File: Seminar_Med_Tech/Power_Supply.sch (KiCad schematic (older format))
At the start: 35 parts, among them U2 LM317T, U3 LM317T, U4 LM317T, U5 LM317T, U6 LM337K

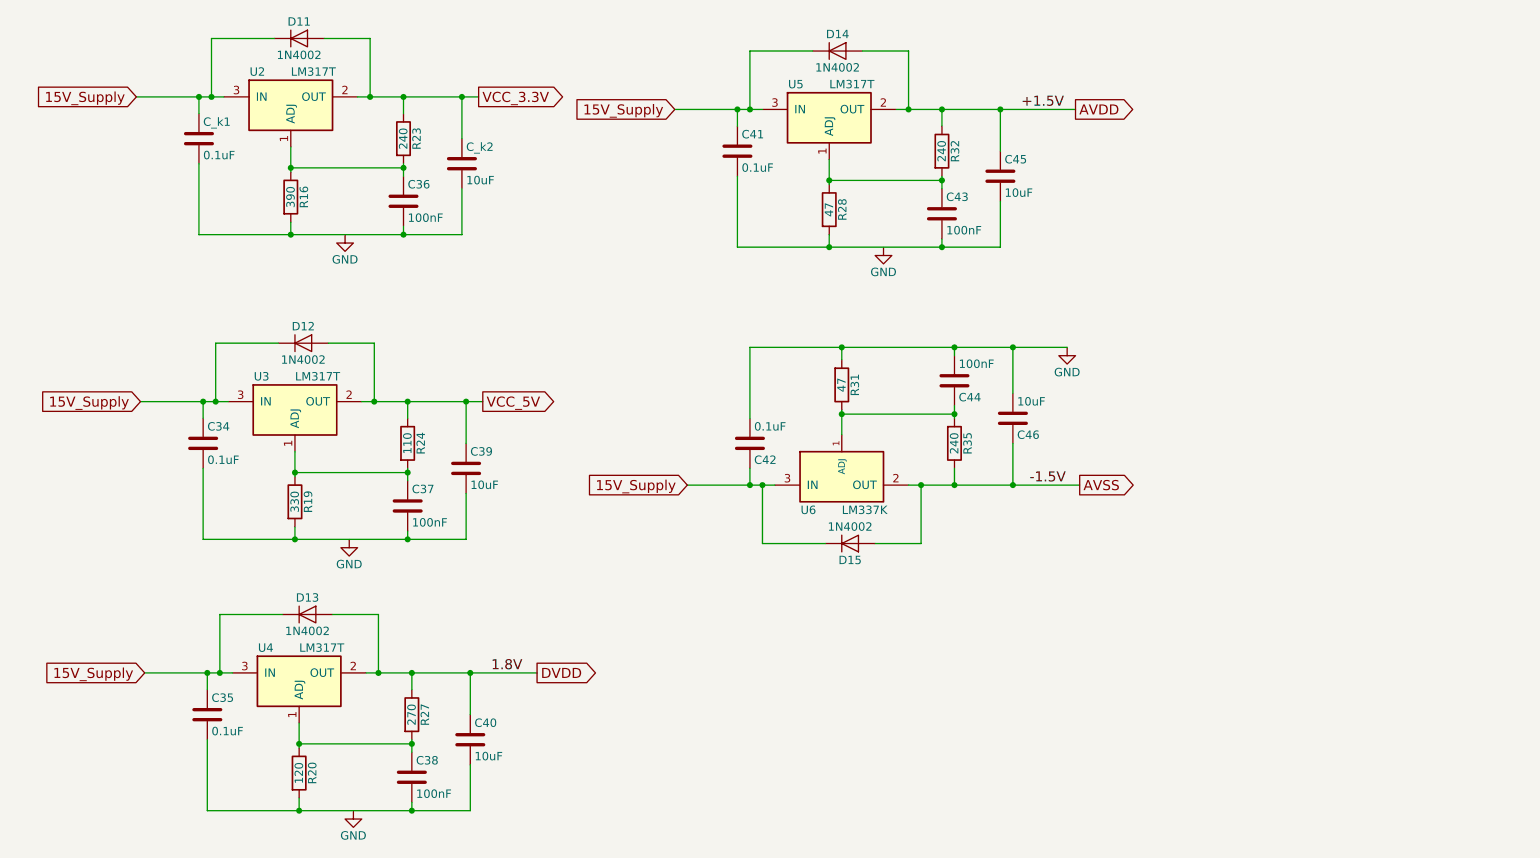
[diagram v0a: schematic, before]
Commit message: Updated Schaltbild and changed BOM
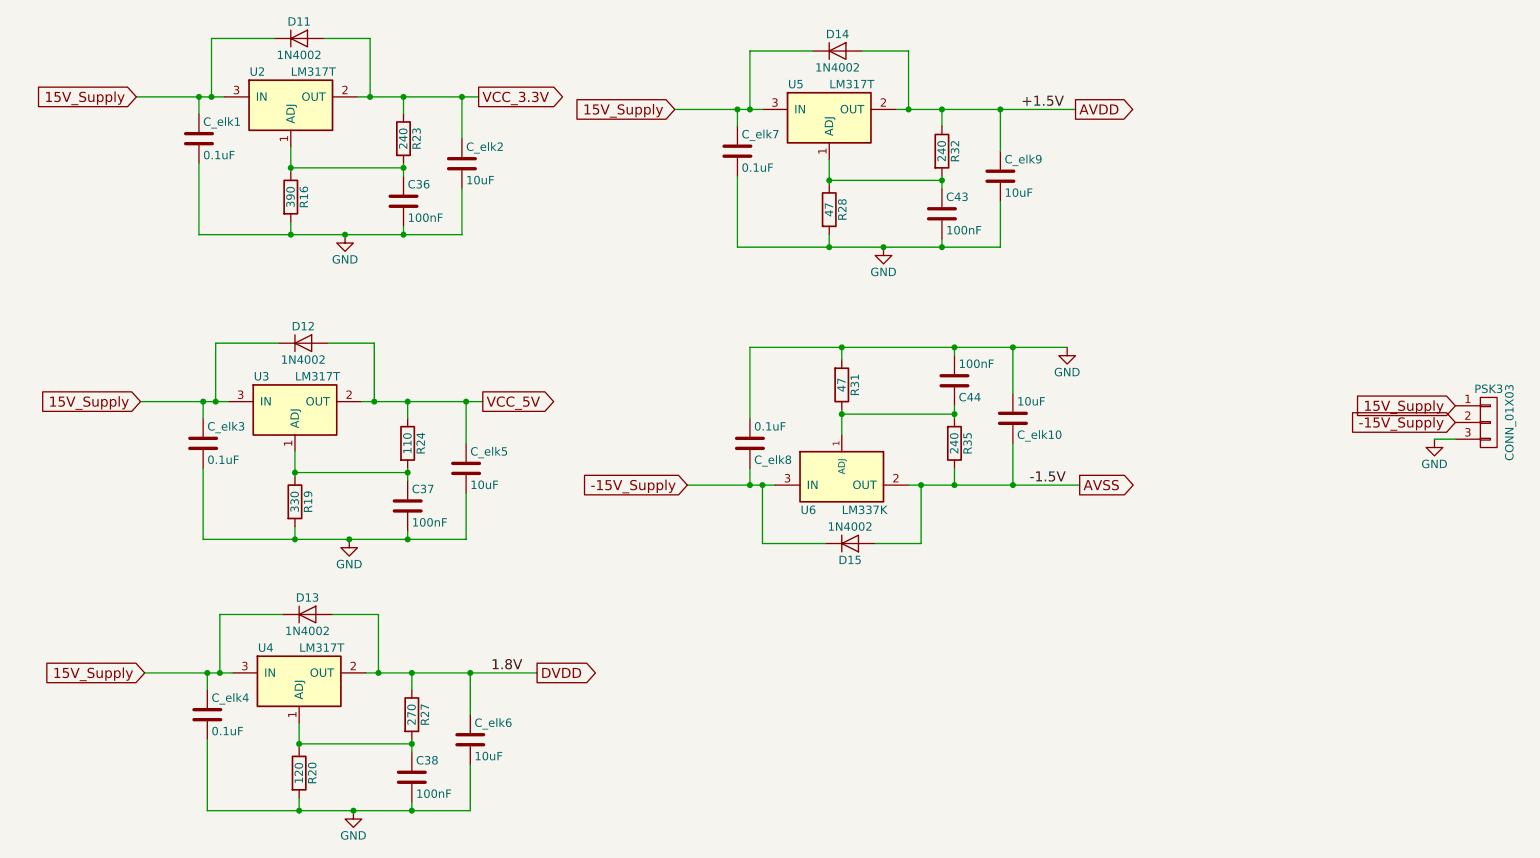
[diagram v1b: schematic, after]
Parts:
- added PSK3: CONN_01X03, symbol CONN_01X03
- renumbered C_k1 to C_elk1, C46 to C_elk10, C_k2 to C_elk2, C34 to C_elk3, C35 to C_elk4, C39 to C_elk5, C40 to C_elk6, C41 to C_elk7, C42 to C_elk8, C45 to C_elk9
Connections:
- net 15V_Supply: now also PSK3.1 (P1); no longer C_elk8.1, D15.1 (K), U6.3 (IN)
- net GND: now also C36.2, C37.2, C38.2, C43.2, C_elk1.2, C_elk2.2, C_elk3.2, C_elk4.2, C_elk5.2, C_elk6.2, C_elk7.2, C_elk9.2, R16.2, R19.2, R20.2, R28.2, PSK3.3 (P3)
- new net -15V_Supply: C_elk8.1, D15.1 (K), PSK3.2 (P2), U6.3 (IN)

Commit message: Updated Schaltbild and added LM317 footprint
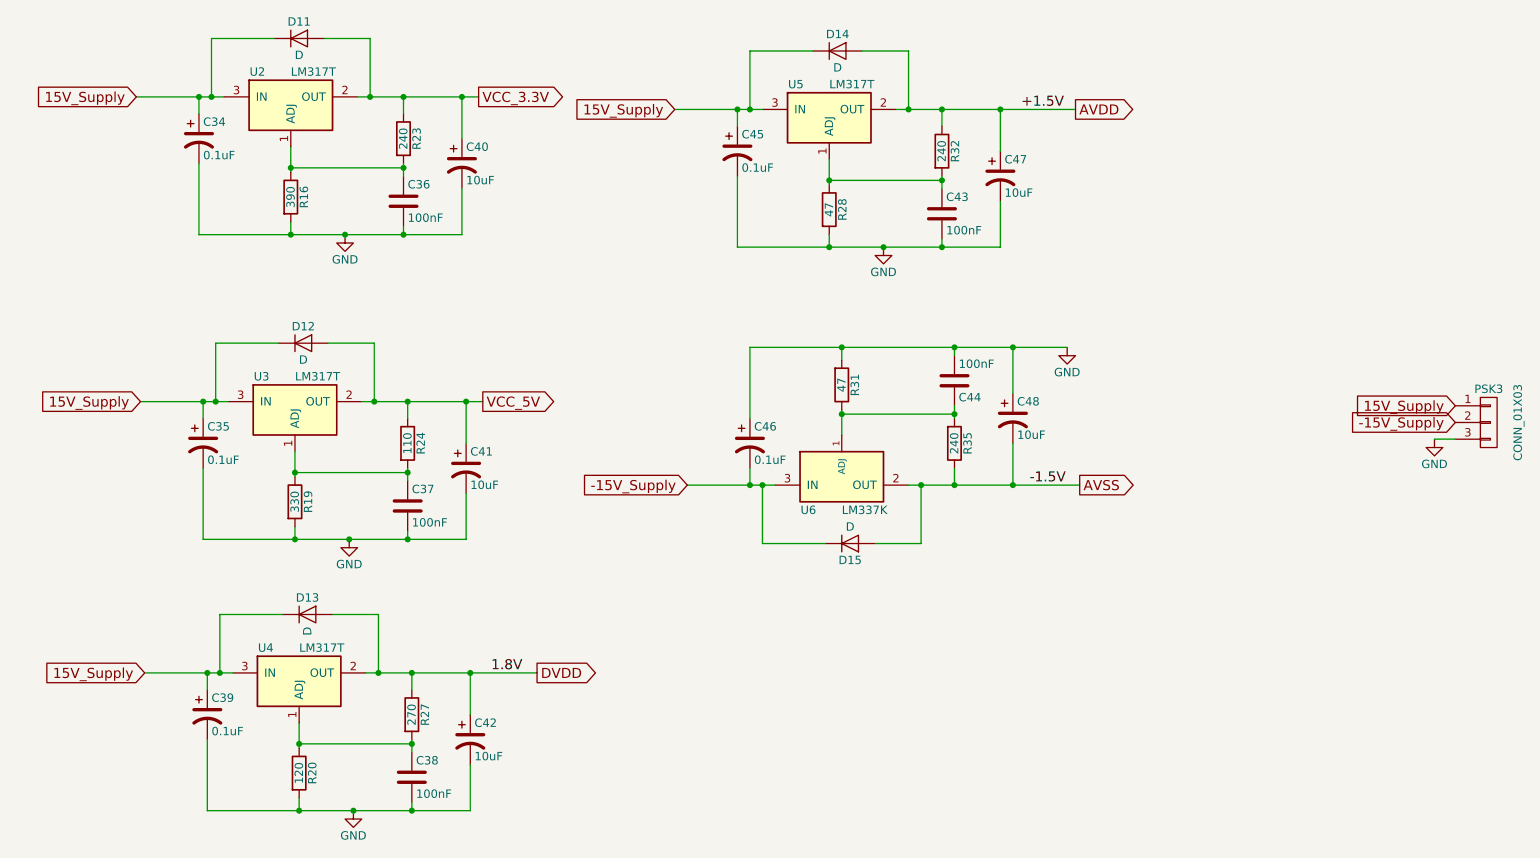
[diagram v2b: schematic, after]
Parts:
- removed C_elk1, C_elk3, C_elk4, C_elk7, C_elk8: 0.1uF, Capacitors_SMD:C_1206_HandSoldering, symbol C
- removed C_elk10, C_elk2, C_elk5, C_elk6, C_elk9: 10uF, Capacitors_SMD:C_1206_HandSoldering, symbol C
- added C34, C35, C39, C45, C46: 0.1uF, Capacitors_SMD:CP_Elec_4x5.8, symbol CP1
- added C40, C41, C42, C47, C48: 10uF, Capacitors_SMD:CP_Elec_4x5.8, symbol CP1
- D11, D12, D13, D14, D15: value 1N4002 -> D
- PSK3: footprint (none) -> Pin_Headers:Pin_Header_Straight_1x03_Pitch2.54mm
- U2, U3, U4, U5: footprint TO_SOT_Packages_THT:TO-220_Vertical -> Linear_Regulator:LM317
- U6: footprint TO_SOT_Packages_THT:TO-3 -> Linear_Regulator:LM317
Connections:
- net -15V_Supply: now also C46.2
- net 15V_Supply: now also C34.1, C35.1, C39.1, C45.1
- net AVDD: now also C47.1
- net AVSS: now also C48.2
- net DVDD: now also C42.1
- net GND: now also C34.2, C35.2, C39.2, C40.2, C41.2, C42.2, C45.2, C46.1, C47.2, C48.1
- net VCC_3.3V: now also C40.1
- net VCC_5V: now also C41.1
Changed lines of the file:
@@
 F 0 "U2" H 2600 1700 50  0000 C CNN
 F 1 "LM317T" H 2800 1700 50  0000 L CNN
-F 2 "TO_SOT_Packages_THT:TO-220_Vertical" H 2800 1600 50  0001 C CIN
+F 2 "Linear_Regulator:LM317" H 2800 1600 50  0001 C CIN
 F 3 "" H 2800 1500 50  0001 C CNN
 	1    2800 1500
-	1    0    0    -1
-$EndComp
-$Comp
-L C C_elk1
-U 1 1 5947F15B
-P 2250 1700
-F 0 "C_elk1" H 2275 1800 50  0000 L CNN
-F 1 "0.1uF" H 2275 1600 50  0000 L CNN
-F 2 "Capacitors_SMD:C_1206_HandSoldering" H 2288 1550 50  0001 C CNN
-F 3 "" H 2250 1700 50  0001 C CNN
-	1    2250 1700
 	1    0    0    -1
 $EndComp
@@
 $EndComp
 $Comp
-L C C_elk2
-U 1 1 5947F1C2
-P 3825 1850
-F 0 "C_elk2" H 3850 1950 50  0000 L CNN
-F 1 "10uF" H 3850 1750 50  0000 L CNN
-F 2 "Capacitors_SMD:C_1206_HandSoldering" H 3863 1700 50  0001 C CNN
-F 3 "" H 3825 1850 50  0001 C CNN
-	1    3825 1850
-	1    0    0    -1
-$EndComp
-$Comp
 L D D11
 U 1 1 5947F210
 P 2850 1100
 F 0 "D11" H 2850 1200 50  0000 C CNN
-F 1 "1N4002" H 2850 1000 50  0000 C CNN
+F 1 "D" H 2850 1000 50  0000 C CNN
 F 2 "Diodes_SMD:D_SC-80_HandSoldering" H 2850 1100 50  0001 C CNN
 F 3 "" H 2850 1100 50  0001 C CNN
@@
 F 0 "U3" H 2625 3525 50  0000 C CNN
 F 1 "LM317T" H 2825 3525 50  0000 L CNN
-F 2 "TO_SOT_Packages_THT:TO-220_Vertical" H 2825 3425 50  0001 C CIN
+F 2 "Linear_Regulator:LM317" H 2825 3425 50  0001 C CIN
 F 3 "" H 2825 3325 50  0001 C CNN
 	1    2825 3325
-	1    0    0    -1
-$EndComp
-$Comp
-L C C_elk3
-U 1 1 59480213
-P 2275 3525
-F 0 "C_elk3" H 2300 3625 50  0000 L CNN
-F 1 "0.1uF" H 2300 3425 50  0000 L CNN
-F 2 "Capacitors_SMD:C_1206_HandSoldering" H 2313 3375 50  0001 C CNN
-F 3 "" H 2275 3525 50  0001 C CNN
-	1    2275 3525
 	1    0    0    -1
 $EndComp
@@
 $EndComp
 $Comp
-L C C_elk5
-U 1 1 5948021F
-P 3850 3675
-F 0 "C_elk5" H 3875 3775 50  0000 L CNN
-F 1 "10uF" H 3875 3575 50  0000 L CNN
-F 2 "Capacitors_SMD:C_1206_HandSoldering" H 3888 3525 50  0001 C CNN
-F 3 "" H 3850 3675 50  0001 C CNN
-	1    3850 3675
-	1    0    0    -1
-$EndComp
-$Comp
 L D D12
 U 1 1 59480225
 P 2875 2925
 F 0 "D12" H 2875 3025 50  0000 C CNN
-F 1 "1N4002" H 2875 2825 50  0000 C CNN
+F 1 "D" H 2875 2825 50  0000 C CNN
 F 2 "Diodes_SMD:D_SC-80_HandSoldering" H 2875 2925 50  0001 C CNN
 F 3 "" H 2875 2925 50  0001 C CNN
@@
 F 0 "U5" H 5825 1775 50  0000 C CNN
 F 1 "LM317T" H 6025 1775 50  0000 L CNN
-F 2 "TO_SOT_Packages_THT:TO-220_Vertical" H 6025 1675 50  0001 C CIN
+F 2 "Linear_Regulator:LM317" H 6025 1675 50  0001 C CIN
 F 3 "" H 6025 1575 50  0001 C CNN
 	1    6025 1575
-	1    0    0    -1
-$EndComp
-$Comp
-L C C_elk7
-U 1 1 59480A0E
-P 5475 1775
-F 0 "C_elk7" H 5500 1875 50  0000 L CNN
-F 1 "0.1uF" H 5500 1675 50  0000 L CNN
-F 2 "Capacitors_SMD:C_1206_HandSoldering" H 5513 1625 50  0001 C CNN
-F 3 "" H 5475 1775 50  0001 C CNN
-	1    5475 1775
 	1    0    0    -1
 $EndComp
@@
 $EndComp
 $Comp
-L C C_elk9
-U 1 1 59480A1A
-P 7050 1925
-F 0 "C_elk9" H 7075 2025 50  0000 L CNN
-F 1 "10uF" H 7075 1825 50  0000 L CNN
-F 2 "Capacitors_SMD:C_1206_HandSoldering" H 7088 1775 50  0001 C CNN
-F 3 "" H 7050 1925 50  0001 C CNN
-	1    7050 1925
-	1    0    0    -1
-$EndComp
-$Comp
 L D D14
 U 1 1 59480A20
 P 6075 1175
 F 0 "D14" H 6075 1275 50  0000 C CNN
-F 1 "1N4002" H 6075 1075 50  0000 C CNN
+F 1 "D" H 6075 1075 50  0000 C CNN
 F 2 "Diodes_SMD:D_SC-80_HandSoldering" H 6075 1175 50  0001 C CNN
 F 3 "" H 6075 1175 50  0001 C CNN
@@
 F 0 "U4" H 2650 5150 50  0000 C CNN
 F 1 "LM317T" H 2850 5150 50  0000 L CNN
-F 2 "TO_SOT_Packages_THT:TO-220_Vertical" H 2850 5050 50  0001 C CIN
+F 2 "Linear_Regulator:LM317" H 2850 5050 50  0001 C CIN
 F 3 "" H 2850 4950 50  0001 C CNN
 	1    2850 4950
-	1    0    0    -1
-$EndComp
-$Comp
-L C C_elk4
-U 1 1 59480B41
-P 2300 5150
-F 0 "C_elk4" H 2325 5250 50  0000 L CNN
-F 1 "0.1uF" H 2325 5050 50  0000 L CNN
-F 2 "Capacitors_SMD:C_1206_HandSoldering" H 2338 5000 50  0001 C CNN
-F 3 "" H 2300 5150 50  0001 C CNN
-	1    2300 5150
 	1    0    0    -1
 $EndComp
@@
 $EndComp
 $Comp
-L C C_elk6
-U 1 1 59480B4D
-P 3875 5300
-F 0 "C_elk6" H 3900 5400 50  0000 L CNN
-F 1 "10uF" H 3900 5200 50  0000 L CNN
-F 2 "Capacitors_SMD:C_1206_HandSoldering" H 3913 5150 50  0001 C CNN
-F 3 "" H 3875 5300 50  0001 C CNN
-	1    3875 5300
-	1    0    0    -1
-$EndComp
-$Comp
 L D D13
 U 1 1 59480B53
 P 2900 4550
 F 0 "D13" H 2900 4650 50  0000 C CNN
-F 1 "1N4002" H 2900 4450 50  0000 C CNN
+F 1 "D" V 2900 4450 50  0000 C CNN
 F 2 "Diodes_SMD:D_SC-80_HandSoldering" H 2900 4550 50  0001 C CNN
 F 3 "" H 2900 4550 50  0001 C CNN
@@
 F 0 "U6" H 5900 3525 50  0000 C CNN
 F 1 "LM337K" H 6100 3525 50  0000 L CNN
-F 2 "TO_SOT_Packages_THT:TO-3" H 6100 3625 50  0001 C CIN
+F 2 "Linear_Regulator:LM317" H 6100 3625 50  0001 C CIN
 F 3 "" H 6100 3725 50  0001 C CNN
 	1    6100 3725
@@
 Text GLabel 5175 3775 0    60   Input ~ 0
 -15V_Supply
-$Comp
-L C C_elk8
-U 1 1 5948C0A3
-P 5550 3525
-F 0 "C_elk8" H 5575 3625 50  0000 L CNN
-F 1 "0.1uF" H 5575 3425 50  0000 L CNN
-F 2 "Capacitors_SMD:C_1206_HandSoldering" H 5588 3375 50  0001 C CNN
-F 3 "" H 5550 3525 50  0001 C CNN
-	1    5550 3525
-	1    0    0    1
-$EndComp
 $Comp
 L C C44
@@
 $EndComp
 $Comp
-L C C_elk10
-U 1 1 5948C0AF
-P 7125 3375
-F 0 "C_elk10" H 7150 3475 50  0000 L CNN
-F 1 "10uF" H 7150 3275 50  0000 L CNN
-F 2 "Capacitors_SMD:C_1206_HandSoldering" H 7163 3225 50  0001 C CNN
-F 3 "" H 7125 3375 50  0001 C CNN
-	1    7125 3375
-	1    0    0    1
-$EndComp
-$Comp
 L D D15
 U 1 1 5948C0B5
 P 6150 4125
 F 0 "D15" H 6150 4225 50  0000 C CNN
-F 1 "1N4002" H 6150 4025 50  0000 C CNN
+F 1 "D" H 6150 4025 50  0000 C CNN
 F 2 "Diodes_SMD:D_SC-80_HandSoldering" H 6150 4125 50  0001 C CNN
 F 3 "" H 6150 4125 50  0001 C CNN
@@
 P 9975 3400
 F 0 "PSK3" H 9975 3600 50  0000 C CNN
-F 1 "CONN_01X03" V 10100 3400 50  0000 C CNN
-F 2 "" H 9975 3400 50  0001 C CNN
+F 1 "CONN_01X03" V 10150 3400 50  0000 C CNN
+F 2 "Pin_Headers:Pin_Header_Straight_1x03_Pitch2.54mm" H 9975 3400 50  0001 C CNN
 F 3 "" H 9975 3400 50  0001 C CNN
 	1    9975 3400
@@
 Wire Wire Line
 	9775 3500 9650 3500
+$Comp
+L CP1 C34
+U 1 1 594A8579
+P 2250 1700
+F 0 "C34" H 2275 1800 50  0000 L CNN
+F 1 "0.1uF" H 2275 1600 50  0000 L CNN
+F 2 "Capacitors_SMD:CP_Elec_4x5.8" H 2250 1700 50  0001 C CNN
+F 3 "" H 2250 1700 50  0001 C CNN
+	1    2250 1700
+	1    0    0    -1
+$EndComp
+$Comp
+L CP1 C40
+U 1 1 594A8C56
+P 3825 1850
+F 0 "C40" H 3850 1950 50  0000 L CNN
+F 1 "10uF" H 3850 1750 50  0000 L CNN
+F 2 "Capacitors_SMD:CP_Elec_4x5.8" H 3825 1850 50  0001 C CNN
+F 3 "" H 3825 1850 50  0001 C CNN
+	1    3825 1850
+	1    0    0    -1
+$EndComp
+$Comp
+L CP1 C35
+U 1 1 594AC0E4
+P 2275 3525
+F 0 "C35" H 2300 3625 50  0000 L CNN
+F 1 "0.1uF" H 2300 3425 50  0000 L CNN
+F 2 "Capacitors_SMD:CP_Elec_4x5.8" H 2275 3525 50  0001 C CNN
+F 3 "" H 2275 3525 50  0001 C CNN
+	1    2275 3525
+	1    0    0    -1
+$EndComp
+$Comp
+L CP1 C39
+U 1 1 594AC187
+P 2300 5150
+F 0 "C39" H 2325 5250 50  0000 L CNN
+F 1 "0.1uF" H 2325 5050 50  0000 L CNN
+F 2 "Capacitors_SMD:CP_Elec_4x5.8" H 2300 5150 50  0001 C CNN
+F 3 "" H 2300 5150 50  0001 C CNN
+	1    2300 5150
+	1    0    0    -1
+$EndComp
+$Comp
+L CP1 C45
+U 1 1 594AC237
+P 5475 1775
+F 0 "C45" H 5500 1875 50  0000 L CNN
+F 1 "0.1uF" H 5500 1675 50  0000 L CNN
+F 2 "Capacitors_SMD:CP_Elec_4x5.8" H 5475 1775 50  0001 C CNN
+F 3 "" H 5475 1775 50  0001 C CNN
+	1    5475 1775
+	1    0    0    -1
+$EndComp
+$Comp
+L CP1 C46
+U 1 1 594AC2F8
+P 5550 3525
+F 0 "C46" H 5575 3625 50  0000 L CNN
+F 1 "0.1uF" H 5575 3425 50  0000 L CNN
+F 2 "Capacitors_SMD:CP_Elec_4x5.8" H 5550 3525 50  0001 C CNN
+F 3 "" H 5550 3525 50  0001 C CNN
+	1    5550 3525
+	1    0    0    -1
+$EndComp
+$Comp
+L CP1 C41
+U 1 1 594AC3B8
+P 3850 3675
+F 0 "C41" H 3875 3775 50  0000 L CNN
+F 1 "10uF" H 3875 3575 50  0000 L CNN
+F 2 "Capacitors_SMD:CP_Elec_4x5.8" H 3850 3675 50  0001 C CNN
+F 3 "" H 3850 3675 50  0001 C CNN
+	1    3850 3675
+	1    0    0    -1
+$EndComp
+$Comp
+L CP1 C42
+U 1 1 594AC487
+P 3875 5300
+F 0 "C42" H 3900 5400 50  0000 L CNN
+F 1 "10uF" H 3900 5200 50  0000 L CNN
+F 2 "Capacitors_SMD:CP_Elec_4x5.8" H 3875 5300 50  0001 C CNN
+F 3 "" H 3875 5300 50  0001 C CNN
+	1    3875 5300
+	1    0    0    -1
+$EndComp
+$Comp
+L CP1 C47
+U 1 1 594AC565
+P 7050 1925
+F 0 "C47" H 7075 2025 50  0000 L CNN
+F 1 "10uF" H 7075 1825 50  0000 L CNN
+F 2 "Capacitors_SMD:CP_Elec_4x5.8" H 7050 1925 50  0001 C CNN
+F 3 "" H 7050 1925 50  0001 C CNN
+	1    7050 1925
+	1    0    0    -1
+$EndComp
+$Comp
+L CP1 C48
+U 1 1 594AC65A
+P 7125 3375
+F 0 "C48" H 7150 3475 50  0000 L CNN
+F 1 "10uF" H 7150 3275 50  0000 L CNN
+F 2 "Capacitors_SMD:CP_Elec_4x5.8" H 7125 3375 50  0001 C CNN
+F 3 "" H 7125 3375 50  0001 C CNN
+	1    7125 3375
+	1    0    0    -1
+$EndComp
 $EndSCHEMATC

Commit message: Update
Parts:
- C36, C37, C38, C43, C44: value 100nF -> 0.1uF
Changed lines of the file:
@@
 P 3475 2075
 F 0 "C36" H 3500 2175 50  0000 L CNN
-F 1 "100nF" H 3500 1975 50  0000 L CNN
+F 1 "0.1uF" H 3500 1975 50  0000 L CNN
 F 2 "Capacitors_SMD:C_1206_HandSoldering" H 3513 1925 50  0001 C CNN
 F 3 "" H 3475 2075 50  0001 C CNN
@@
 P 3500 3900
 F 0 "C37" H 3525 4000 50  0000 L CNN
-F 1 "100nF" H 3525 3800 50  0000 L CNN
+F 1 "0.1uF" H 3525 3800 50  0000 L CNN
 F 2 "Capacitors_SMD:C_1206_HandSoldering" H 3538 3750 50  0001 C CNN
 F 3 "" H 3500 3900 50  0001 C CNN
@@
 P 6700 2150
 F 0 "C43" H 6725 2250 50  0000 L CNN
-F 1 "100nF" H 6725 2050 50  0000 L CNN
+F 1 "0.1uF" H 6725 2050 50  0000 L CNN
 F 2 "Capacitors_SMD:C_1206_HandSoldering" H 6738 2000 50  0001 C CNN
 F 3 "" H 6700 2150 50  0001 C CNN
@@
 P 3525 5525
 F 0 "C38" H 3550 5625 50  0000 L CNN
-F 1 "100nF" H 3550 5425 50  0000 L CNN
+F 1 "0.1uF" H 3550 5425 50  0000 L CNN
 F 2 "Capacitors_SMD:C_1206_HandSoldering" H 3563 5375 50  0001 C CNN
 F 3 "" H 3525 5525 50  0001 C CNN
@@
 P 6775 3150
 F 0 "C44" H 6800 3250 50  0000 L CNN
-F 1 "100nF" H 6800 3050 50  0000 L CNN
+F 1 "0.1uF" H 6800 3050 50  0000 L CNN
 F 2 "Capacitors_SMD:C_1206_HandSoldering" H 6813 3000 50  0001 C CNN
 F 3 "" H 6775 3150 50  0001 C CNN
